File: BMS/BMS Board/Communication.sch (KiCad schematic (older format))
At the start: 9 parts, among them J1 10129379-904002BLF

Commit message: changed ui components to be classes instead of methods in Screen class
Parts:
- removed O21: TLP2270_TP4,E, SOIC127P1105X220-8N, symbol SamacSys_Parts:TLP2270_TP4,E
- added C?: 0805ZC104MAT2A, CAPC2012X94N, symbol SamacSys_Parts:0805ZC104MAT2A
- added IC? (x2): TLP2310_TPL,E, SOIC127P700X220-6N, symbol SamacSys_Parts:TLP2310_TPL,E
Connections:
- net labels added: 3v3
- wire segments 18 -> 20
- no-connect marks 0 -> 2
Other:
- moved on the sheet: C17, J1, LED1, LED2, R114, R115, R116, R117

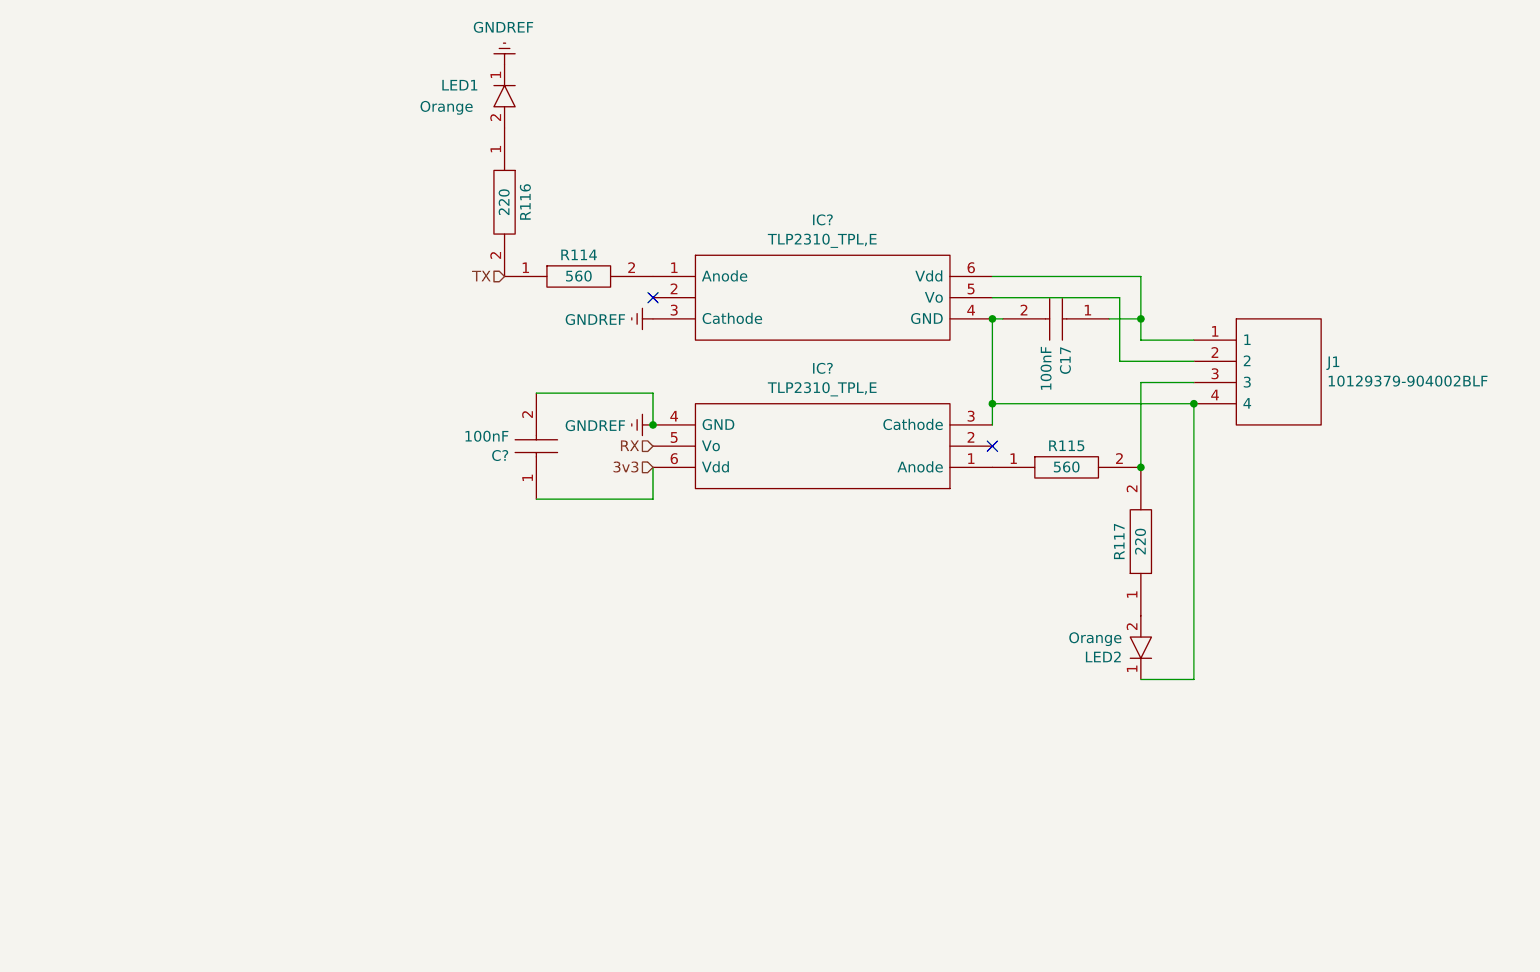
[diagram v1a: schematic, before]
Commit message: "SingleDigitNumberSelector" now blinks when idle.
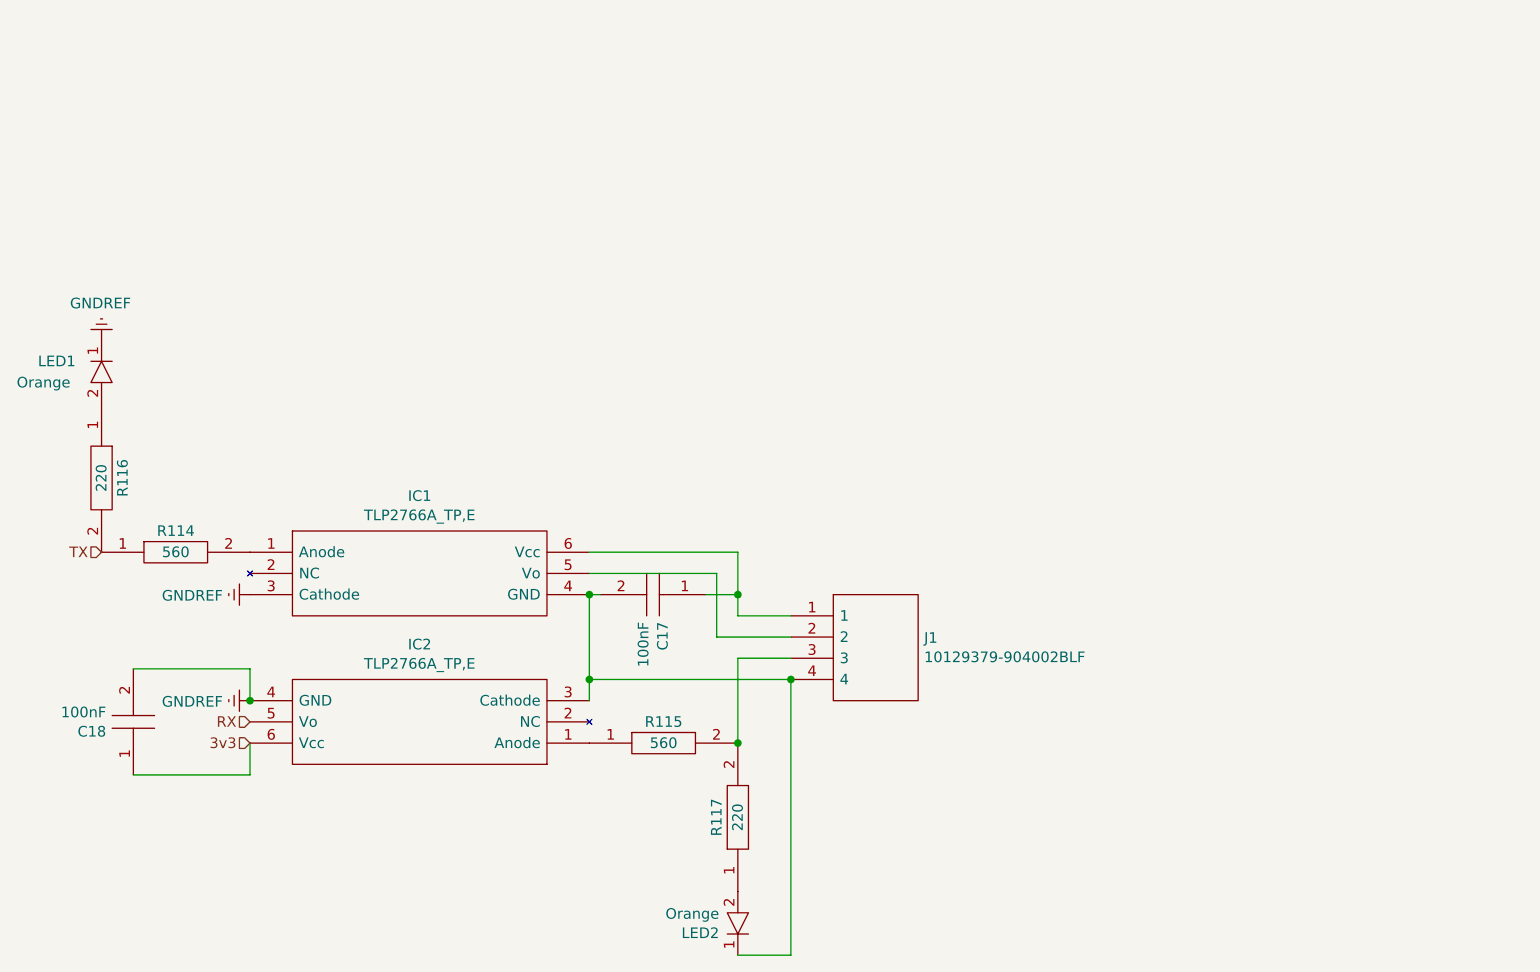
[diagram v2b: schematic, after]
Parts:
- removed IC? (x2): TLP2310_TPL,E, SOIC127P700X220-6N, symbol SamacSys_Parts:TLP2310_TPL,E
- added IC1, IC2: TLP2766A_TP,E, SOT127P1000X230-6N, symbol SamacSys_Parts:TLP2766A_TP,E
- gave numbers to parts that had none: 1
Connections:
- net 3v3: now also IC2.6 (Vcc)
- net GNDREF: now also IC1.3 (Cathode), IC2.4 (GND)
- net RX: now also IC2.5 (Vo)
- net at R115.1: now also IC2.1 (Anode)
- net at R114.2: now also IC1.1 (Anode)
- net at C17.1, J1.1: now also IC1.6 (Vcc)
- net at C17.2, J1.4, LED2.1: now also IC1.4 (GND), IC2.3 (Cathode)
- net at J1.2: now also IC1.5 (Vo)
- no-connect marks 2 -> 0
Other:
- moved on the sheet: C17, C18, J1, LED1, LED2, R114, R115, R116, R117

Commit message: ...
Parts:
- removed R114, R115: ERJ-6ENF5600V, RESC2012X70N, symbol SamacSys_Parts:ERJ-6ENF5600V
- added R114, R115: ERJ-P06F2200V, RESC2012X70N, symbol SamacSys_Parts:ERJ-P06F2200V
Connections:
- net TX: now also R114.1
- net at IC2.1 (Anode): now also R115.1
- net at J1.3, R117.2: now also R115.2
- net at IC1.1 (Anode): now also R114.2
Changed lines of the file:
@@
 RX
-$Comp
-L SamacSys_Parts:ERJ-6ENF5600V R115
-U 1 1 5EEB44FF
-P 4900 5850
-F 0 "R115" H 4900 5950 50  0000 C CNN
-F 1 "ERJ-6ENF5600V" H 4750 5600 50  0001 L CNN
-F 2 "RESC2012X70N" H 4750 5500 50  0001 L CNN
-F 3 "https://componentsearchengine.com/Datasheets/1/ERJ-6ENF5600V.pdf" H 5100 5800 50  0001 L CNN
-F 4 "Thick Film Resistors - SMD 0805 560ohms 1% AEC-Q200" H 4750 5400 50  0001 L CNN "Description"
-F 5 "0.7" H 4750 5300 50  0001 L CNN "Height"
-F 6 "667-ERJ-6ENF5600V" H 4750 5200 50  0001 L CNN "Mouser Part Number"
-F 7 "https://www.mouser.com/Search/Refine.aspx?Keyword=667-ERJ-6ENF5600V" H 4750 5100 50  0001 L CNN "Mouser Price/Stock"
-F 8 "Panasonic" H 4750 5000 50  0001 L CNN "Manufacturer_Name"
-F 9 "ERJ-6ENF5600V" H 4750 4900 50  0001 L CNN "Manufacturer_Part_Number"
-F 10 "560" H 4900 5850 50  0000 C CNN "Resistance"
-	1    4900 5850
-	1    0    0    -1
-$EndComp
-$Comp
-L SamacSys_Parts:ERJ-6ENF5600V R114
-U 1 1 5EEB4D6E
-P 2600 4950
-F 0 "R114" H 2600 5050 50  0000 C CNN
-F 1 "ERJ-6ENF5600V" H 2450 4700 50  0001 L CNN
-F 2 "RESC2012X70N" H 2450 4600 50  0001 L CNN
-F 3 "https://componentsearchengine.com/Datasheets/1/ERJ-6ENF5600V.pdf" H 2800 4900 50  0001 L CNN
-F 4 "Thick Film Resistors - SMD 0805 560ohms 1% AEC-Q200" H 2450 4500 50  0001 L CNN "Description"
-F 5 "0.7" H 2450 4400 50  0001 L CNN "Height"
-F 6 "667-ERJ-6ENF5600V" H 2450 4300 50  0001 L CNN "Mouser Part Number"
-F 7 "https://www.mouser.com/Search/Refine.aspx?Keyword=667-ERJ-6ENF5600V" H 2450 4200 50  0001 L CNN "Mouser Price/Stock"
-F 8 "Panasonic" H 2450 4100 50  0001 L CNN "Manufacturer_Name"
-F 9 "ERJ-6ENF5600V" H 2450 4000 50  0001 L CNN "Manufacturer_Part_Number"
-F 10 "560" H 2600 4950 50  0000 C CNN "Resistance"
-	1    2600 4950
-	1    0    0    -1
-$EndComp
 $Comp
 L SamacSys_Parts:0805ZC104MAT2A C17
@@
 Wire Wire Line
 	2950 6000 2400 6000
-Connection ~ 5250 5850
 Wire Wire Line
 	5500 5550 5500 6850
@@
 $EndComp
 Connection ~ 2950 5650
+$Comp
+L SamacSys_Parts:ERJ-P06F2200V R114
+U 1 1 5EF1FB3D
+P 2600 4950
+F 0 "R114" H 2600 5050 50  0000 C CNN
+F 1 "ERJ-P06F2200V" H 2450 4700 50  0001 L CNN
+F 2 "RESC2012X70N" H 2450 4600 50  0001 L CNN
+F 3 "https://componentsearchengine.com/Datasheets/1/ERJ-P06F2200V.pdf" H 2800 4900 50  0001 L CNN
+F 4 "Thick Film Resistors - SMD 0805 220ohms 0.5W 1% AEC-Q200" H 2450 4500 50  0001 L CNN "Description"
+F 5 "0.7" H 2450 4400 50  0001 L CNN "Height"
+F 6 "667-ERJ-P06F2200V" H 2450 4300 50  0001 L CNN "Mouser Part Number"
+F 7 "https://www.mouser.com/Search/Refine.aspx?Keyword=667-ERJ-P06F2200V" H 2450 4200 50  0001 L CNN "Mouser Price/Stock"
+F 8 "Panasonic" H 2450 4100 50  0001 L CNN "Manufacturer_Name"
+F 9 "ERJ-P06F2200V" H 2450 4000 50  0001 L CNN "Manufacturer_Part_Number"
+F 10 "220" H 2600 4950 50  0000 C CNN "Resistance"
+	1    2600 4950
+	1    0    0    -1
+$EndComp
+$Comp
+L SamacSys_Parts:ERJ-P06F2200V R115
+U 1 1 5EF2060E
+P 4900 5850
+F 0 "R115" H 4900 5950 50  0000 C CNN
+F 1 "ERJ-P06F2200V" H 4750 5600 50  0001 L CNN
+F 2 "RESC2012X70N" H 4750 5500 50  0001 L CNN
+F 3 "https://componentsearchengine.com/Datasheets/1/ERJ-P06F2200V.pdf" H 5100 5800 50  0001 L CNN
+F 4 "Thick Film Resistors - SMD 0805 220ohms 0.5W 1% AEC-Q200" H 4750 5400 50  0001 L CNN "Description"
+F 5 "0.7" H 4750 5300 50  0001 L CNN "Height"
+F 6 "667-ERJ-P06F2200V" H 4750 5200 50  0001 L CNN "Mouser Part Number"
+F 7 "https://www.mouser.com/Search/Refine.aspx?Keyword=667-ERJ-P06F2200V" H 4750 5100 50  0001 L CNN "Mouser Price/Stock"
+F 8 "Panasonic" H 4750 5000 50  0001 L CNN "Manufacturer_Name"
+F 9 "ERJ-P06F2200V" H 4750 4900 50  0001 L CNN "Manufacturer_Part_Number"
+F 10 "220" H 4900 5850 50  0000 C CNN "Resistance"
+	1    4900 5850
+	1    0    0    -1
+$EndComp
+Connection ~ 5250 5850
 $EndSCHEMATC
